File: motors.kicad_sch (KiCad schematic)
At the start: 20 parts, among them J5 1769, J6 1769, J7 1769, J8 1769, Q1 BSS138, Q2 BSS138, Q3 BSS138, Q4 BSS138

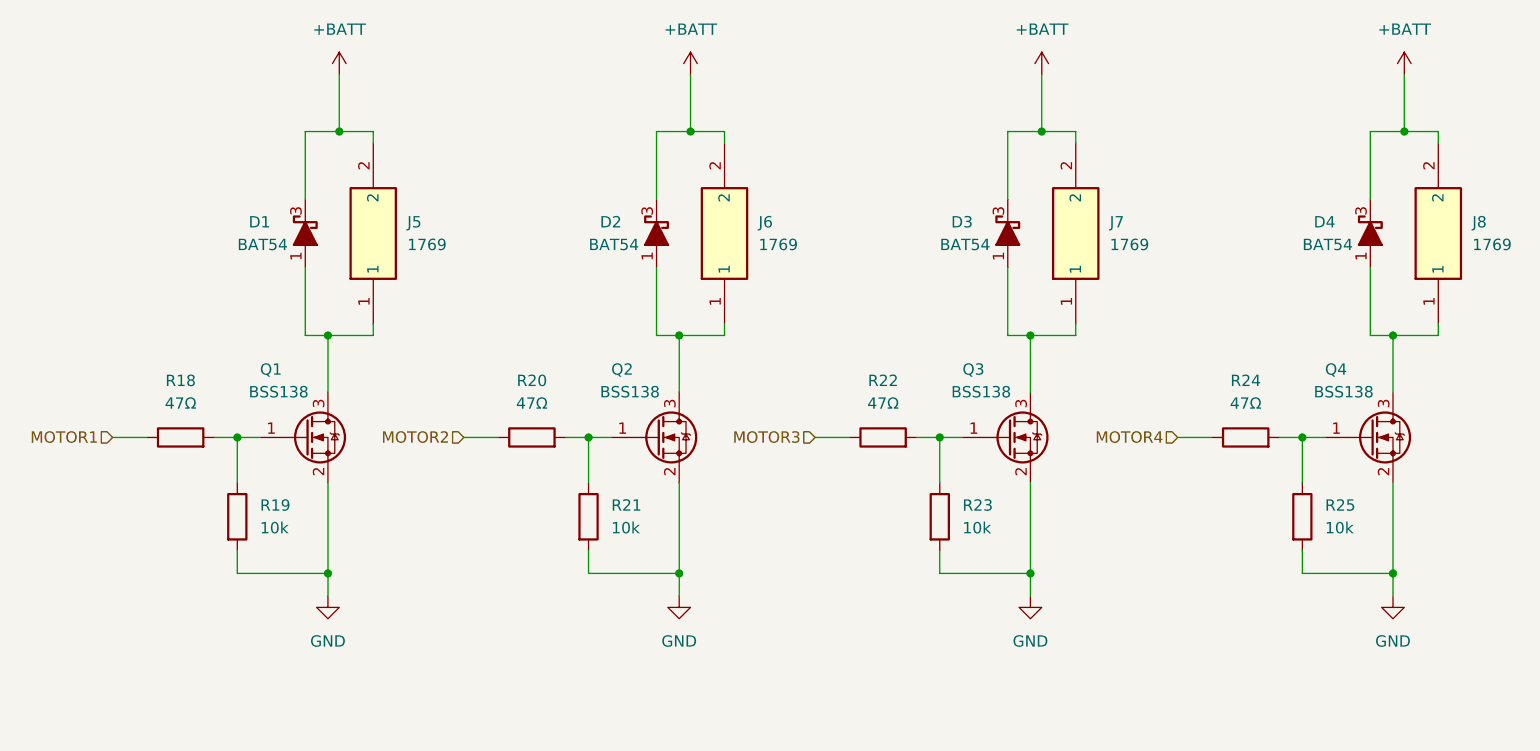
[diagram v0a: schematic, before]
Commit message: Added FPGA power component
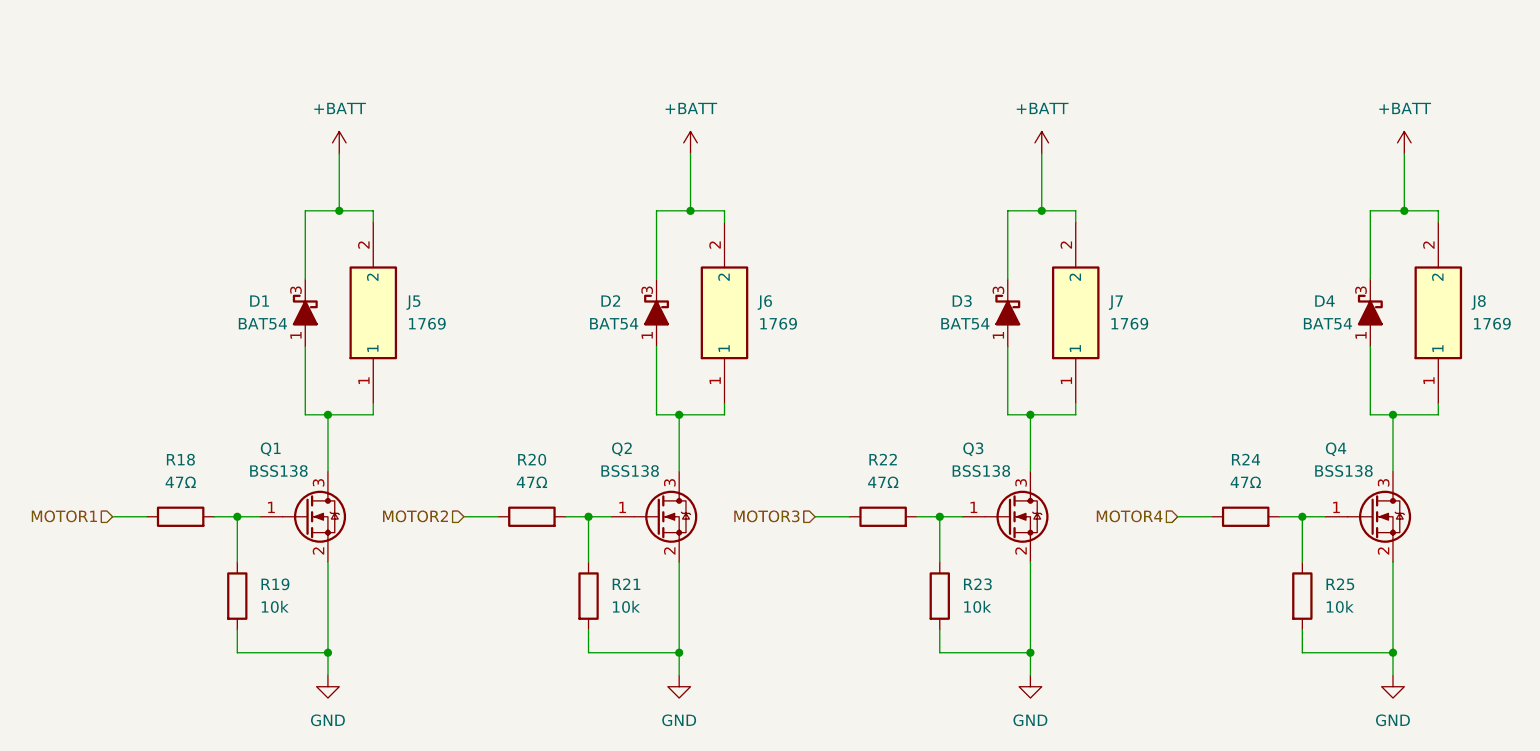
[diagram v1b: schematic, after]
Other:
- title: (none) -> Motors
- moved on the sheet: D1, D2, D3, D4, J5, J6, J7, J8, Q1, Q2, Q3, Q4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

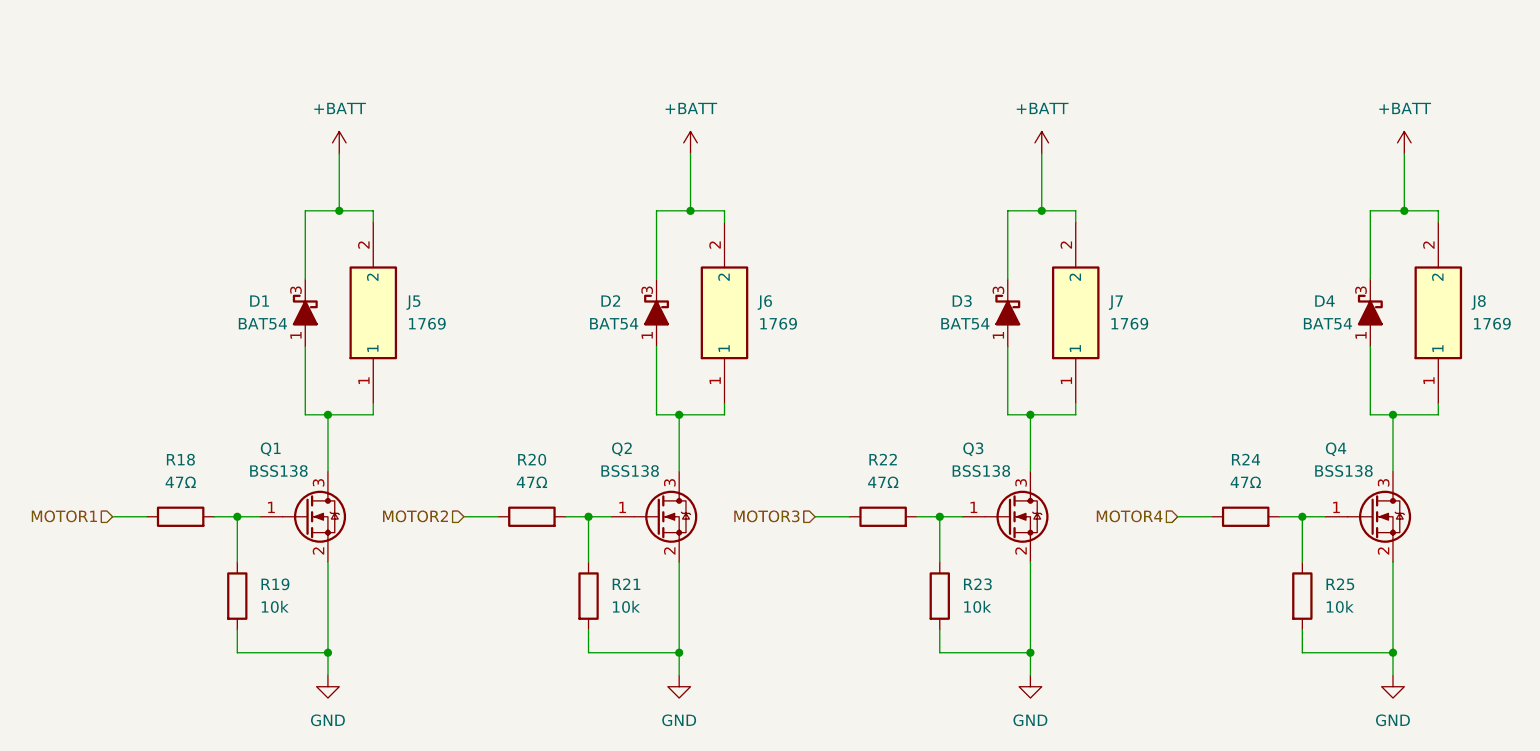
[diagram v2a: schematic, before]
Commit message: Replacing global power labels with hierarchical pins
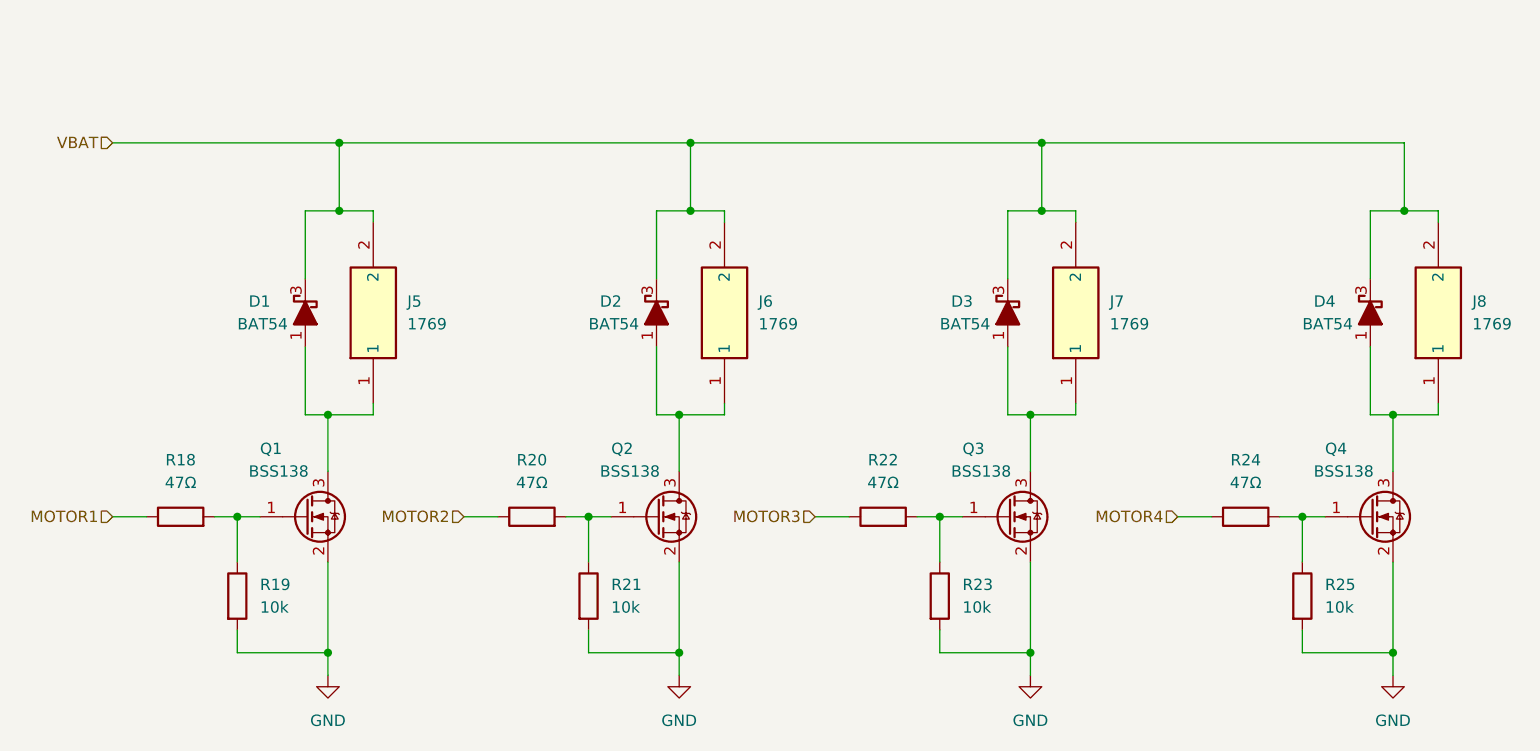
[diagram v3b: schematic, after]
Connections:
- net +BATT renamed VBAT
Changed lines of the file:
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@@
   (junction (at 129.54 35.56) (diameter 0) (color 0 0 0 0)
   )
+  (junction (at 50.8 27.94) (diameter 0) (color 0 0 0 0)
+  )
   (junction (at 49.53 58.42) (diameter 0) (color 0 0 0 0)
   )
@@
   (junction (at 168.91 58.42) (diameter 0) (color 0 0 0 0)
   )
+  (junction (at 129.54 27.94) (diameter 0) (color 0 0 0 0)
+  )
+  (junction (at 90.17 27.94) (diameter 0) (color 0 0 0 0)
+  )
   (junction (at 128.27 58.42) (diameter 0) (color 0 0 0 0)
   )
@@
     (stroke (width 0) (type default))
   )
-  (wire (pts (xy 170.18 29.21) (xy 170.18 35.56))
+  (wire (pts (xy 170.18 27.94) (xy 170.18 35.56))
     (stroke (width 0) (type default))
   )
@@
     (stroke (width 0) (type default))
   )
+  (wire (pts (xy 25.4 27.94) (xy 50.8 27.94))
+    (stroke (width 0) (type default))
+  )
   (wire (pts (xy 54.61 35.56) (xy 54.61 36.83))
     (stroke (width 0) (type default))
@@
     (stroke (width 0) (type default))
   )
+  (wire (pts (xy 170.18 27.94) (xy 129.54 27.94))
+    (stroke (width 0) (type default))
+  )
   (wire (pts (xy 158.75 69.85) (xy 161.29 69.85))
     (stroke (width 0) (type default))
@@
     (stroke (width 0) (type default))
   )
-  (wire (pts (xy 129.54 29.21) (xy 129.54 35.56))
+  (wire (pts (xy 129.54 27.94) (xy 129.54 35.56))
     (stroke (width 0) (type default))
   )
@@
     (stroke (width 0) (type default))
   )
-  (wire (pts (xy 50.8 29.21) (xy 50.8 35.56))
+  (wire (pts (xy 50.8 27.94) (xy 50.8 35.56))
     (stroke (width 0) (type default))
   )
@@
     (stroke (width 0) (type default))
   )
-  (wire (pts (xy 90.17 29.21) (xy 90.17 35.56))
+  (wire (pts (xy 90.17 27.94) (xy 90.17 35.56))
     (stroke (width 0) (type default))
   )
@@
     (stroke (width 0) (type default))
   )
+  (wire (pts (xy 129.54 27.94) (xy 90.17 27.94))
+    (stroke (width 0) (type default))
+  )
   (wire (pts (xy 166.37 58.42) (xy 166.37 50.8))
     (stroke (width 0) (type default))
@@
   )
   (wire (pts (xy 25.4 69.85) (xy 29.21 69.85))
+    (stroke (width 0) (type default))
+  )
+  (wire (pts (xy 90.17 27.94) (xy 50.8 27.94))
     (stroke (width 0) (type default))
   )
@@
   )
   (hierarchical_label "MOTOR3" (shape input) (at 104.14 69.85 180) (fields_autoplaced)
+    (effects (font (size 1.27 1.27)) (justify right))
+  )
+  (hierarchical_label "VBAT" (shape input) (at 25.4 27.94 180) (fields_autoplaced)
     (effects (font (size 1.27 1.27)) (justify right))
   )
@@
     )
   )
-  (symbol (lib_id "power:+BATT") (at 90.17 29.21 0) (unit 1)
-    (in_bom yes) (on_board yes) (dnp no) (fields_autoplaced)
-    (property "Reference" "#PWR031" (at 90.17 33.02 0)
-      (effects (font (size 1.27 1.27)) hide)
-    )
-    (property "Value" "+BATT" (at 90.17 24.13 0)
-      (effects (font (size 1.27 1.27)))
-    )
-    (property "Footprint" "" (at 90.17 29.21 0)
-      (effects (font (size 1.27 1.27)) hide)
-    )
-    (property "Datasheet" "" (at 90.17 29.21 0)
-      (effects (font (size 1.27 1.27)) hide)
-    )
-    (pin "1")
-    (instances
-      (project "drone"
-        (path "/a9d9e6e7-8403-4088-be51-8a69908fe001/63f46230-c13b-4098-bd2e-201c446eeb4f"
-          (reference "#PWR031") (unit 1)
-        )
-      )
-      (project "MOTORS"
-        (path "/b89fe223-6396-4bbc-9cf8-0bc602b84ef9"
-          (reference "#PWR?") (unit 1)
-        )
-      )
-      (project "drone"
-        (path "/d34d8324-c983-4098-8d7e-5c2fbd34794d/3a965de9-a8eb-46d2-baf1-071b0ab3526c"
-          (reference "#PWR07") (unit 1)
-        )
-      )
-    )
-  )
   (symbol (lib_id "PCM_4ms_Resistor:47R_0402") (at 111.76 69.85 90) (unit 1)
     (in_bom yes) (on_board yes) (dnp no) (fields_autoplaced)
@@
     )
   )
-  (symbol (lib_id "power:+BATT") (at 129.54 29.21 0) (unit 1)
-    (in_bom yes) (on_board yes) (dnp no) (fields_autoplaced)
-    (property "Reference" "#PWR033" (at 129.54 33.02 0)
-      (effects (font (size 1.27 1.27)) hide)
-    )
-    (property "Value" "+BATT" (at 129.54 24.13 0)
-      (effects (font (size 1.27 1.27)))
-    )
-    (property "Footprint" "" (at 129.54 29.21 0)
-      (effects (font (size 1.27 1.27)) hide)
-    )
-    (property "Datasheet" "" (at 129.54 29.21 0)
-      (effects (font (size 1.27 1.27)) hide)
-    )
-    (pin "1")
-    (instances
-      (project "drone"
-        (path "/a9d9e6e7-8403-4088-be51-8a69908fe001/63f46230-c13b-4098-bd2e-201c446eeb4f"
-          (reference "#PWR033") (unit 1)
-        )
-      )
-      (project "MOTORS"
-        (path "/b89fe223-6396-4bbc-9cf8-0bc602b84ef9"
-          (reference "#PWR?") (unit 1)
-        )
-      )
-      (project "drone"
-        (path "/d34d8324-c983-4098-8d7e-5c2fbd34794d/3a965de9-a8eb-46d2-baf1-071b0ab3526c"
-          (reference "#PWR08") (unit 1)
-        )
-      )
-    )
-  )
   (symbol (lib_id "SamacSys_Parts:1769") (at 93.98 57.15 90) (unit 1)
     (in_bom yes) (on_board yes) (dnp no) (fields_autoplaced)
@@
     )
   )
-  (symbol (lib_id "power:+BATT") (at 170.18 29.21 0) (unit 1)
-    (in_bom yes) (on_board yes) (dnp no) (fields_autoplaced)
-    (property "Reference" "#PWR035" (at 170.18 33.02 0)
-      (effects (font (size 1.27 1.27)) hide)
-    )
-    (property "Value" "+BATT" (at 170.18 24.13 0)
-      (effects (font (size 1.27 1.27)))
-    )
-    (property "Footprint" "" (at 170.18 29.21 0)
-      (effects (font (size 1.27 1.27)) hide)
-    )
-    (property "Datasheet" "" (at 170.18 29.21 0)
-      (effects (font (size 1.27 1.27)) hide)
-    )
-    (pin "1")
-    (instances
-      (project "drone"
-        (path "/a9d9e6e7-8403-4088-be51-8a69908fe001/63f46230-c13b-4098-bd2e-201c446eeb4f"
-          (reference "#PWR035") (unit 1)
-        )
-      )
-      (project "MOTORS"
-        (path "/b89fe223-6396-4bbc-9cf8-0bc602b84ef9"
-          (reference "#PWR?") (unit 1)
-        )
-      )
-      (project "drone"
-        (path "/d34d8324-c983-4098-8d7e-5c2fbd34794d/3a965de9-a8eb-46d2-baf1-071b0ab3526c"
-          (reference "#PWR09") (unit 1)
-        )
-      )
-    )
-  )
   (symbol (lib_id "PCM_4ms_Power-symbol:GND") (at 168.91 87.63 0) (unit 1)
     (in_bom yes) (on_board yes) (dnp no) (fields_autoplaced)
@@
         )
       )
-    )
-  )
-  (symbol (lib_id "power:+BATT") (at 50.8 29.21 0) (unit 1)
-    (in_bom yes) (on_board yes) (dnp no) (fields_autoplaced)
-    (property "Reference" "#PWR029" (at 50.8 33.02 0)
-      (effects (font (size 1.27 1.27)) hide)
-    )
-    (property "Value" "+BATT" (at 50.8 24.13 0)
-      (effects (font (size 1.27 1.27)))
-    )
-    (property "Footprint" "" (at 50.8 29.21 0)
-      (effects (font (size 1.27 1.27)) hide)
-    )
-    (property "Datasheet" "" (at 50.8 29.21 0)
-      (effects (font (size 1.27 1.27)) hide)
-    )
-    (pin "1")
-    (instances
-      (project "drone"
-        (path "/a9d9e6e7-8403-4088-be51-8a69908fe001/63f46230-c13b-4098-bd2e-201c446eeb4f"
-          (reference "#PWR029") (unit 1)
-        )
-      )
-      (project "MOTORS"
-        (path "/b89fe223-6396-4bbc-9cf8-0bc602b84ef9"
-          (reference "#PWR?") (unit 1)
-        )
-      )
-      (project "drone"
-        (path "/d34d8324-c983-4098-8d7e-5c2fbd34794d/3a965de9-a8eb-46d2-baf1-071b0ab3526c"
-          (reference "#PWR06") (unit 1)
-        )
-      )

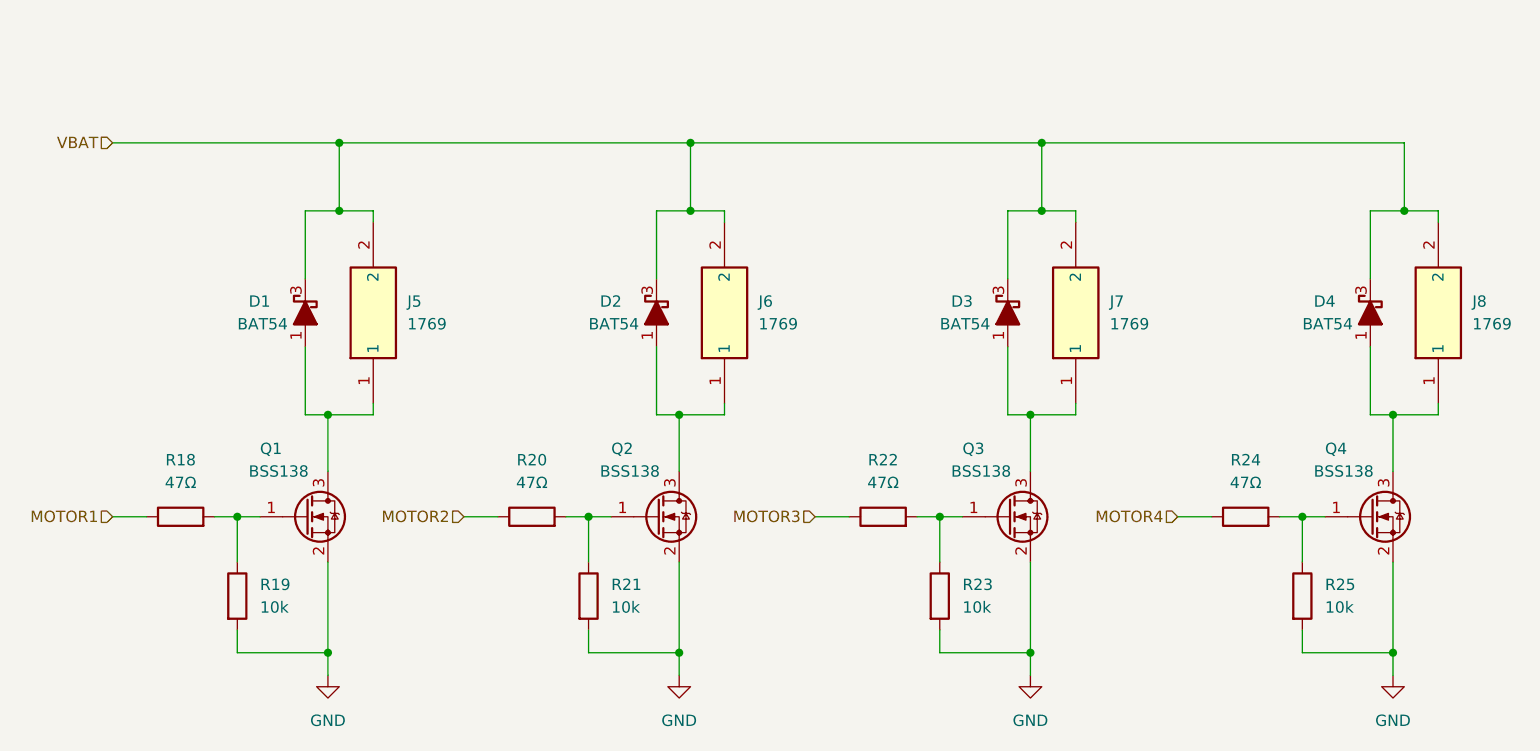
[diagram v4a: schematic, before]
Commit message: Updated KiCad Version of files
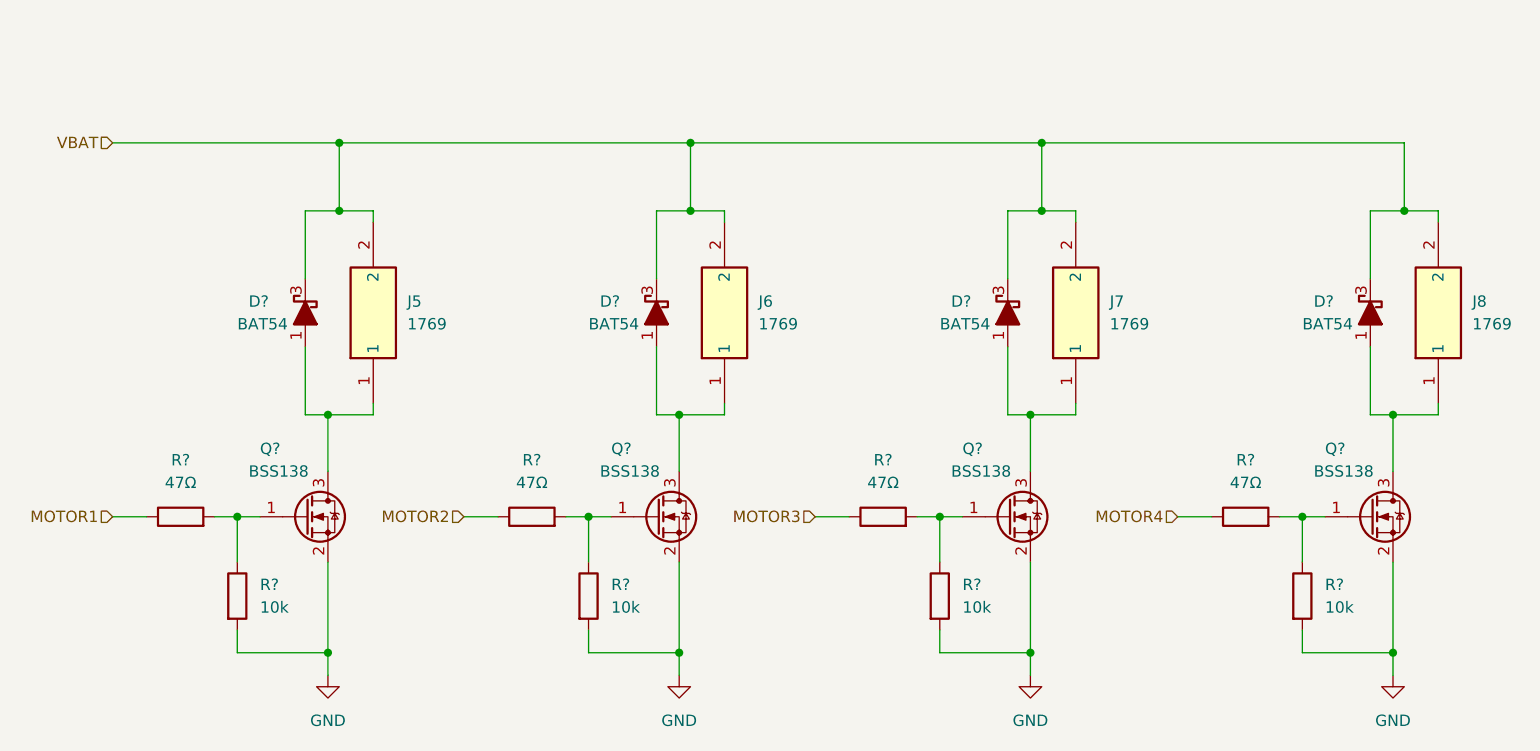
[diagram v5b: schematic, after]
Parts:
- renumbered D2 to D?, D4 to D?, D1 to D?, D3 to D?, Q1 to Q?, Q4 to Q?, Q2 to Q?, Q3 to Q?, R20 to R?, R19 to R?, R18 to R?, R23 to R?, R22 to R?, R21 to R?, R24 to R?, R25 to R?
